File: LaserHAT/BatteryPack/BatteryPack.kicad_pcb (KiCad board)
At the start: 2 copper layers, 100 x 100 mm, 144 parts, among them J1 TYPE-C-31-M-12, J3 B4B-PH-K-S(LF)(SN), J5 S5B-XH-A-1(LF)(SN), J6 S5B-XH-A-1(LF)(SN), J7 XT60PW-M, J8 XT60PW-M, Q1 AO3401A, Q10 AO3400A, Q11 AO3400A, Q12 AO3400A, Q13 AO3401A, Q14 AO3400A, Q15 AO3400A, Q16 AO3400A, Q17 AO3400A, Q18 AO3400A, Q6 AO3401A, Q7 AO3400A, Q8 AO3400A, Q9 AO3400A, SW1 CAX-MTS203M-YB-10.6JL, U1 LM393DR2G, U10 HY2213-BB3A, U11 HY2213-BB3A, U12 HY2213-BB3A, U13 HY2213-BB3A, U14 LM393DR2G, U15 LM393DR2G, U16 CJ431, U2 LM393DR2G, U3 CJ431, U4 CH224A, U5 CN3704, U6 HY2213-BB3A, U7 HY2213-BB3A, U8 HY2213-BB3A, U9 HY2213-BB3A

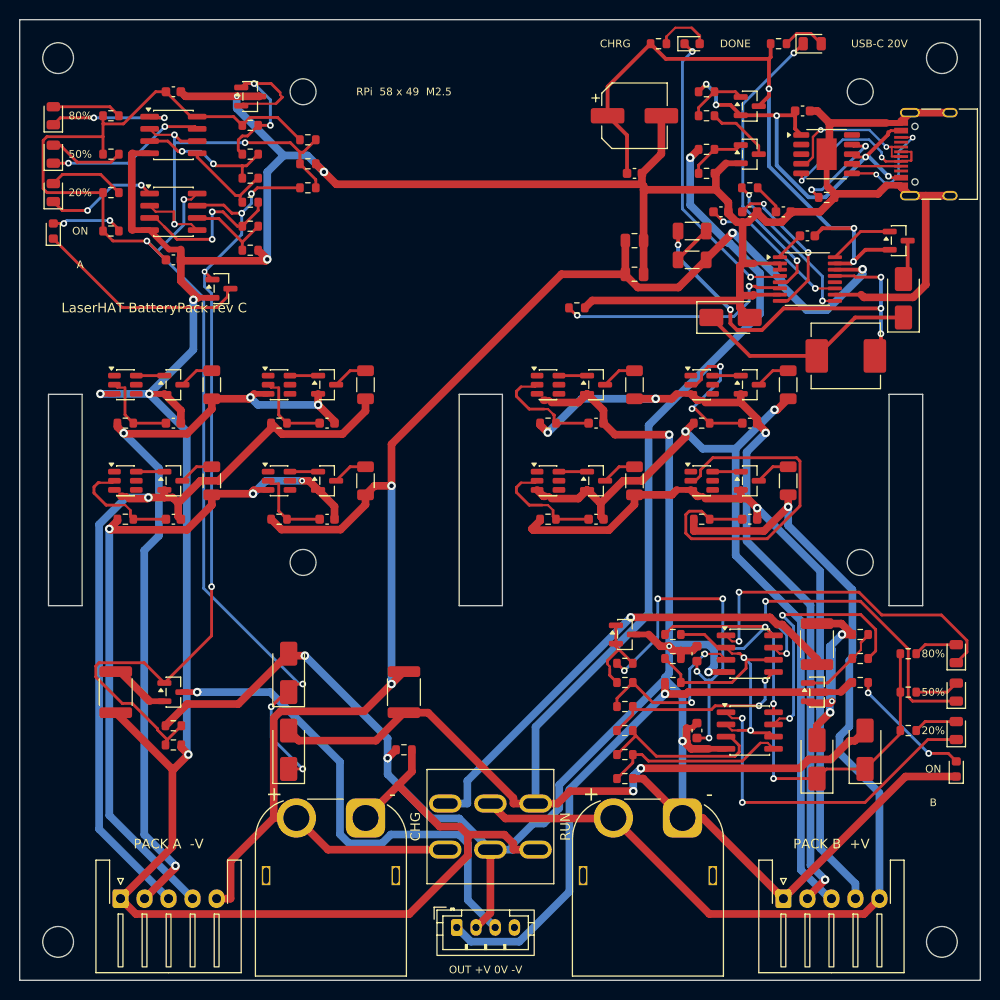
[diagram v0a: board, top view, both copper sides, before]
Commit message: BatteryPack: Pi rests along the front edge (H5-H8 at y 47.5 / 96.5) so the HAT's SW corner is over J3
The e-stim module's battery connector is at the HAT's south-west corner, so the Pi now sits over
y 44-100: toggle (13.5, 61.5, lever along y), J3 (13, 83.5) and chain A in the strip left of the
Pi; J5 left of standoff H7, J7 / J8 / J6 between H7 and H8 (44.5 / 61.5 / 69.5); gauge B LEDs on
the right edge at y 30-42 above the Pi; pack A's right balancer column one row up, clear of H5;
PACK A / B labels on the back silk under the sockets.  Re-routed (Freerouting, 0 unconnected,
stubs trimmed).  DRC 0/0/0, path / sync 0, fab outputs regenerated (136 placements, 44 BOM lines).

Co-Authored-By: Claude Fable 5.1 <noreply@anthropic.com>
Claude-Session: https://claude.ai/code/session_018vgLizGzYPynnY93ajvoVA
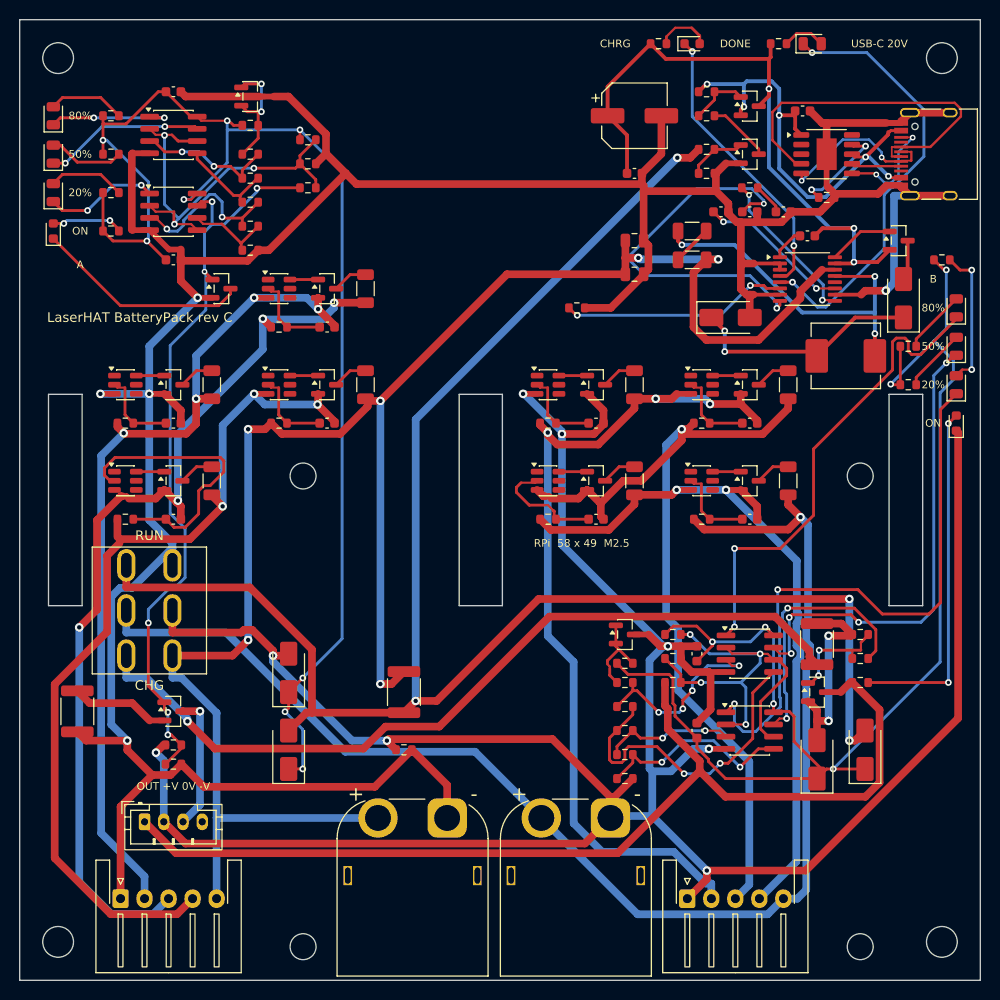
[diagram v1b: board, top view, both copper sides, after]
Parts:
- moved R55 49.1 mm to (96.0, 25.0)
- moved SW1 42.0 mm to (13.5, 61.5), turned to 90 degrees
- moved H5 40.0 mm to (29.5, 47.5)
- moved H6 40.0 mm to (87.5, 47.5)
- moved H7 40.0 mm to (29.5, 96.5)
- moved H8 40.0 mm to (87.5, 96.5)
- moved D11 36.0 mm to (97.5, 42.0)
- moved D12 36.0 mm to (97.5, 38.0)
- moved D13 36.0 mm to (97.5, 34.0)
- moved D14 36.0 mm to (97.5, 30.0)
- moved J3 34.3 mm to (13.0, 83.5)
- moved R56 32.0 mm to (92.5, 38.0)
- moved R57 32.0 mm to (92.5, 34.0)
- moved C13 10.0 mm to (32.0, 32.0)
- moved C15 10.0 mm to (32.0, 42.0)
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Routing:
- net 0V: track 211.1 -> 290.5 mm, vias 6 -> 8
- net +OUT: track 60.4 -> 108.6 mm, vias 1 -> 0
- net +GB: track 93.9 -> 140.4 mm, vias 8 -> 6
- net GND: track 401.4 -> 358.7 mm, vias 7 -> 5
- net /-V: track 51.4 -> 15.6 mm
- net +BATB: track 105.1 -> 140.7 mm
- net +RUN: track 50.5 -> 85.5 mm
- net +CHGB: track 151.2 -> 182.1 mm, vias 3 -> 4
- net Net-(U13-VDD): track 39.4 -> 8.68 mm
- net +BAT: track 168.8 -> 195.8 mm, vias 4 -> 6
- net Net-(D12-K): track 35.7 -> 62.7 mm
- net Net-(D11-A): track 13.2 -> 36.5 mm
- net Net-(U5-COM1): track 16.3 -> 39.3 mm
- net Net-(U4-DP): track 15.8 -> 38.5 mm, vias 2 -> 0
- net /C3: track 74.0 -> 94.8 mm
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
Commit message: BatteryPack: Pi turned 90 degrees along the left edge from the top-left corner
H5-H8 at (3.5 / 52.5, 81.5 / 23.5): the Pi lies over x 0-56, y 0-85 with its header on the
left edge, USB / Ethernet end over the top edge and SD card toward the front; the HAT then
covers x -1..56, y 20-85 and its south-west corner (e-stim module battery connector) is at
(56, 85), the module reaching x 65.  J3 (70, 63) and the toggle (74, 52) sit beside it in the
right column, both gauges' LED columns are on the right edge (B y 30-42, A y 64-76), the four
pack sockets in the front strip; under the Pi only the gauges' comparators (B's moved top
centre), the balancers (B's below A's) and the -V chain (above J7).  place.py has PI_ROT /
pi_xy() so the HAT outline (User.Comments) and Pi outline (User.Drawings) rotate with the
holes; title silk on the back.  Re-routed: Freerouting + maze router for four leftovers, GND
link at U5 pin 10 and three via nudges by hand.  DRC 0/0/0, path / sync 0, fab outputs
regenerated (136 placements, 44 BOM lines).

Co-Authored-By: Claude Fable 5.1 <noreply@anthropic.com>
Claude-Session: https://claude.ai/code/session_018vgLizGzYPynnY93ajvoVA
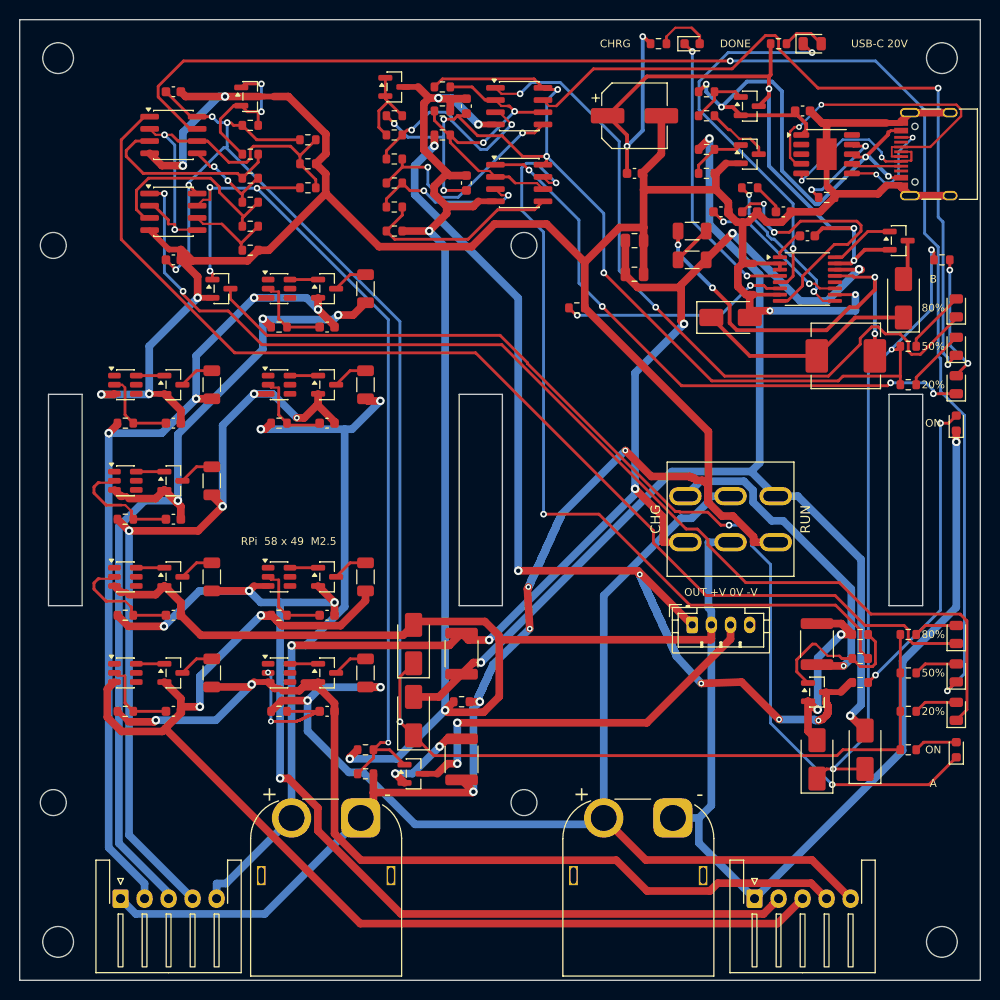
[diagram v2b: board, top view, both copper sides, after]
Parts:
- moved D1 108.4 mm to (97.5, 76.0)
- moved D2 108.4 mm to (97.5, 72.0)
- moved D3 108.4 mm to (97.5, 68.0)
- moved D4 108.4 mm to (97.5, 64.0)
- moved R12 99.0 mm to (92.5, 76.0)
- moved R13 99.0 mm to (92.5, 72.0)
- moved R14 99.0 mm to (92.5, 68.0)
- moved R15 99.0 mm to (92.5, 64.0)
- moved H6 87.4 mm to (3.50, 23.5)
- moved H8 81.0 mm to (52.5, 23.5)
- moved C20 61.8 mm to (46.5, 9.00)
- moved C21 61.8 mm to (46.5, 17.0)
- moved R45 61.8 mm to (39.0, 10.0)
- moved R46 61.8 mm to (39.0, 12.0)
- moved R47 61.8 mm to (39.0, 14.5)
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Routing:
- net Net-(D3-K): track 16.6 -> 153.8 mm
- net Net-(D2-K): track 11.9 -> 119.7 mm
- net Net-(D4-K): track 13.4 -> 120.0 mm, vias 2 -> 0
- net /D1_K: track 22.4 -> 109.0 mm, vias 0 -> 2
- net +CHGB: track 182.1 -> 117.8 mm, vias 4 -> 3
- net /CUT_OCB: track 27.0 -> 84.5 mm
- net +RUN: track 85.5 -> 34.4 mm
- net +G: track 139.7 -> 176.1 mm, vias 8 -> 5
- net GND: track 358.7 -> 394.1 mm, vias 5 -> 12
- net +GB: track 140.4 -> 172.7 mm, vias 6 -> 9
- net /B2: track 90.5 -> 121.4 mm, vias 1 -> 2
- net Net-(D13-K): track 49.6 -> 77.8 mm, vias 4 -> 2
- net /-V: track 15.6 -> 41.8 mm, vias 1 -> 2
- net Net-(D14-K): track 50.4 -> 75.2 mm
- net /B3: track 76.6 -> 100.6 mm
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
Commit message: BatteryPack: Pi turned so its USB-C / HDMI face is flush with the left edge, J3 in the top-left corner under the module's battery pads
The e-stim module hangs 9 mm past the HAT's south edge with its electrode header pointing south, and its battery pads
sit at its SW corner; that face is also the Pi's power / HDMI face.  The Pi now lies along the left edge over x 0-56,
y 15-100 (PI_ROT 270: H5-H8 at (3.5/52.5, 18.5/76.5), SD end up, USB / Ethernet over the front edge), so the
module overhangs the top-left corner (x -9..24, y 16-43) and the stimulation wires and Pi cables all leave over the
left edge instead of crossing the board.  J3 pin 1 at (4, 4), pins down to y 10, right below the module's battery
pads (x -3..3, y 16-23); H1 moved to (12, 4) for it; U15 / C21 to y 27, clear of H5.  The HAT's thumbwheel pokes
past the top edge at x 6.5-19, y 9-15, so the J3 cable stays west of it.  Re-routed (Freerouting, 0 unconnected),
DRC 0 / 0 / 0, path and sync 0, fab outputs and renders regenerated.

Co-Authored-By: Claude Fable 5.1 <noreply@anthropic.com>
Claude-Session: https://claude.ai/code/session_018vgLizGzYPynnY93ajvoVA
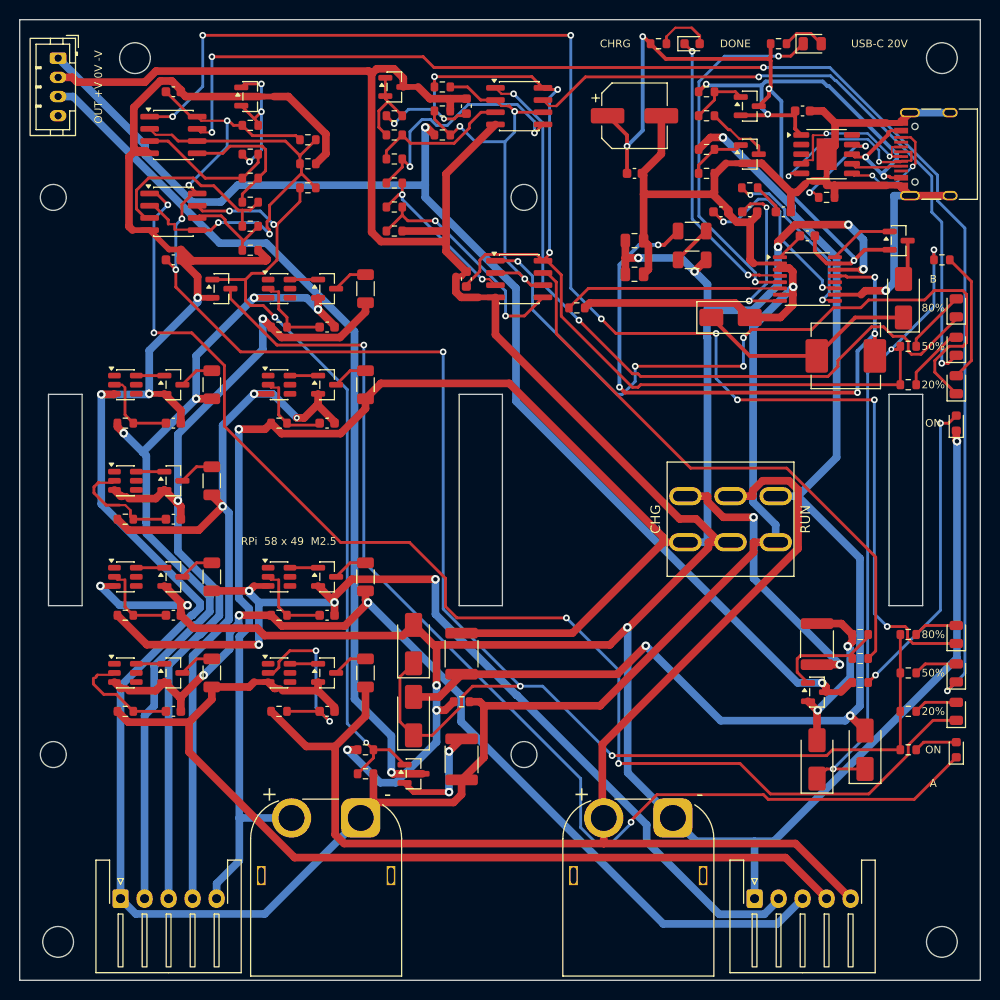
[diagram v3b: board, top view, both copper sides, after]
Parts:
- moved J3 88.5 mm to (4.00, 4.00), turned to -90 degrees
- moved H5 79.8 mm to (52.5, 18.5)
- moved H7 79.8 mm to (3.50, 18.5)
- moved H6 72.2 mm to (52.5, 76.5)
- moved H8 72.2 mm to (3.50, 76.5)
- moved C21 10.0 mm to (46.5, 27.0)
- moved U15 10.0 mm to (52.0, 27.0)
- moved H1 8.00 mm to (12.0, 4.00)
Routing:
- net /-V: track 41.8 -> 91.8 mm, vias 2 -> 1
- net 0V: track 291.5 -> 333.3 mm, vias 6 -> 7
- net Net-(D4-K): track 120.0 -> 148.6 mm, vias 0 -> 8
- net GND: track 394.1 -> 421.0 mm, vias 12 -> 5
- net +BAT: track 186.4 -> 211.6 mm, vias 8 -> 6
- net /CUT_OCB: track 84.5 -> 60.9 mm, vias 2 -> 0
- net /B2: track 121.4 -> 98.9 mm, vias 2 -> 3
- net /CSP: track 42.7 -> 64.6 mm, vias 4 -> 5
- net +OUT: track 106.2 -> 127.8 mm, vias 6 -> 2
- net Net-(U4-DP): track 34.5 -> 16.2 mm
- net Net-(D12-K): track 62.2 -> 77.7 mm
- net Net-(D2-K): track 119.7 -> 134.6 mm, vias 2 -> 4
- net +BATB: track 122.5 -> 135.0 mm, vias 2 -> 0
- net Net-(U5-COM1): track 28.4 -> 16.7 mm
- net /D1_K: track 109.0 -> 120.4 mm
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
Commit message: BatteryPack: toggle turned 90 degrees so its lever is parallel to the Pi (RUN up, CHARGE down)
SW1 at (74, 52) rot 90; re-routed (Freerouting + a hand-drawn front-layer link for U5 pad 10's GND, south of the
charger's pads to the GND trunk at x 75.5).  DRC 0 / 0 / 0, path and sync 0, fab outputs and renders regenerated.

Co-Authored-By: Claude Fable 5.1 <noreply@anthropic.com>
Claude-Session: https://claude.ai/code/session_018vgLizGzYPynnY93ajvoVA
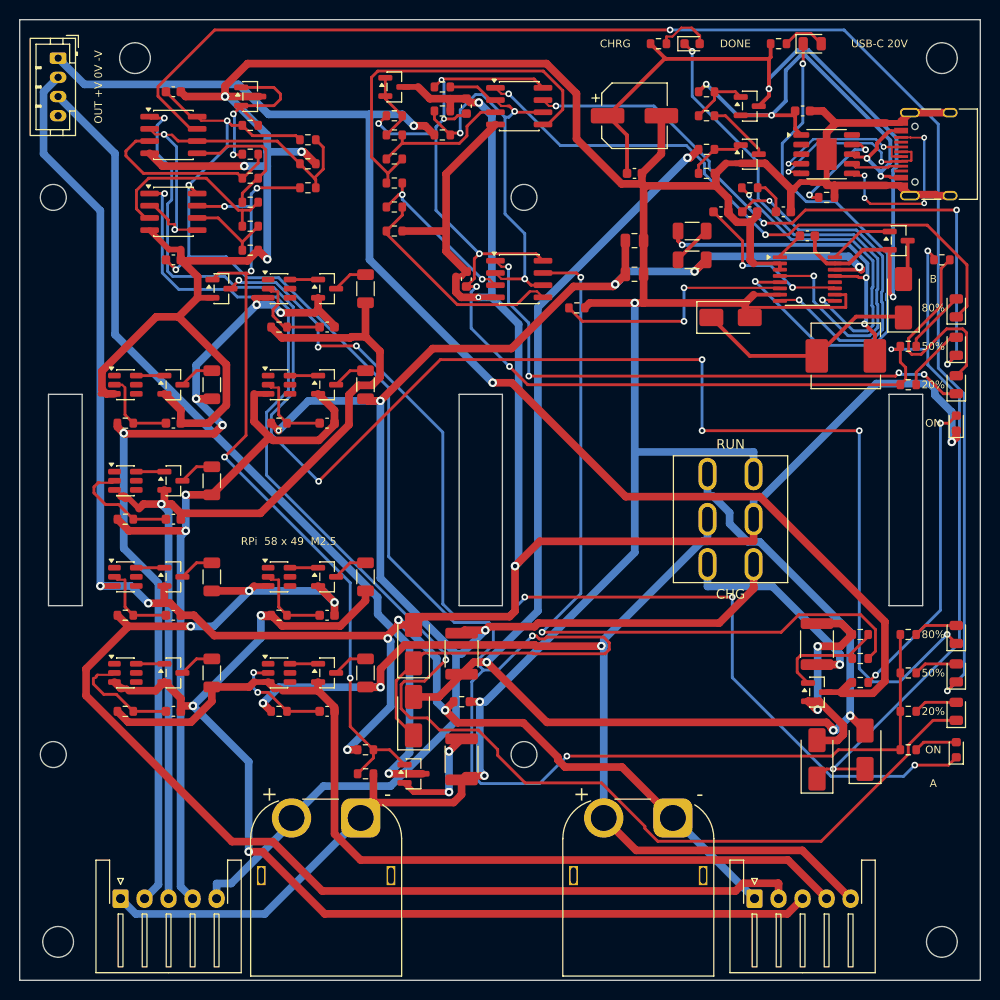
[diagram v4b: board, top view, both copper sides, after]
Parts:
- turned SW1 to 90 degrees
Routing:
- net +G: track 184.1 -> 215.3 mm, vias 7 -> 5
- net /CSP: track 64.6 -> 35.2 mm, vias 5 -> 3
- net +BATB: track 135.0 -> 107.0 mm, vias 0 -> 3
- net /CHRG: track 30.2 -> 56.3 mm
- net Net-(U5-COM1): track 16.7 -> 38.2 mm
- net +BAT: track 211.6 -> 190.3 mm
- net /CUT_OCB: track 60.9 -> 82.2 mm, vias 0 -> 2
- net /B1: track 105.5 -> 126.4 mm, vias 4 -> 3
- net +CHGB: track 128.5 -> 147.9 mm, vias 3 -> 4
- net /DONE: track 38.3 -> 57.0 mm
- net Net-(D12-K): track 77.7 -> 59.4 mm
- net /B2: track 98.9 -> 116.4 mm
- net VCHG: track 72.3 -> 86.9 mm, vias 4 -> 2
- net /TH50B: track 25.8 -> 39.6 mm, vias 2 -> 0
- net +OUT: track 127.8 -> 141.4 mm
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
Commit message: BatteryPack: gauge A's LEDs on the top edge beside its comparators, ICs turned by an orientation pass; re-routed
Gauge A's four LED nets ran ~150 mm each from its comparators (top left) to the right edge: D1-D4 now on the top edge at
x 20-32 with R12-R15 in a column at x 35, labels under them.  An orientation pass (ROT in place.py) tries every IC /
transistor at 0/90/180/270 and keeps the rotation with the shortest ratsnest that overlaps no courtyard (17 parts, ~1 mm
each).  Track 4486 -> 3812 mm, 1253 -> 1121 segments, 143 -> 137 vias.  Freerouting + a hand-drawn link for U5 pad 10's
GND (east, down the back layer, across to the GND trunk at x 76.4).  DRC 0 / 0 / 0, path and sync 0, fab outputs and
renders regenerated.

Co-Authored-By: Claude Fable 5.1 <noreply@anthropic.com>
Claude-Session: https://claude.ai/code/session_018vgLizGzYPynnY93ajvoVA
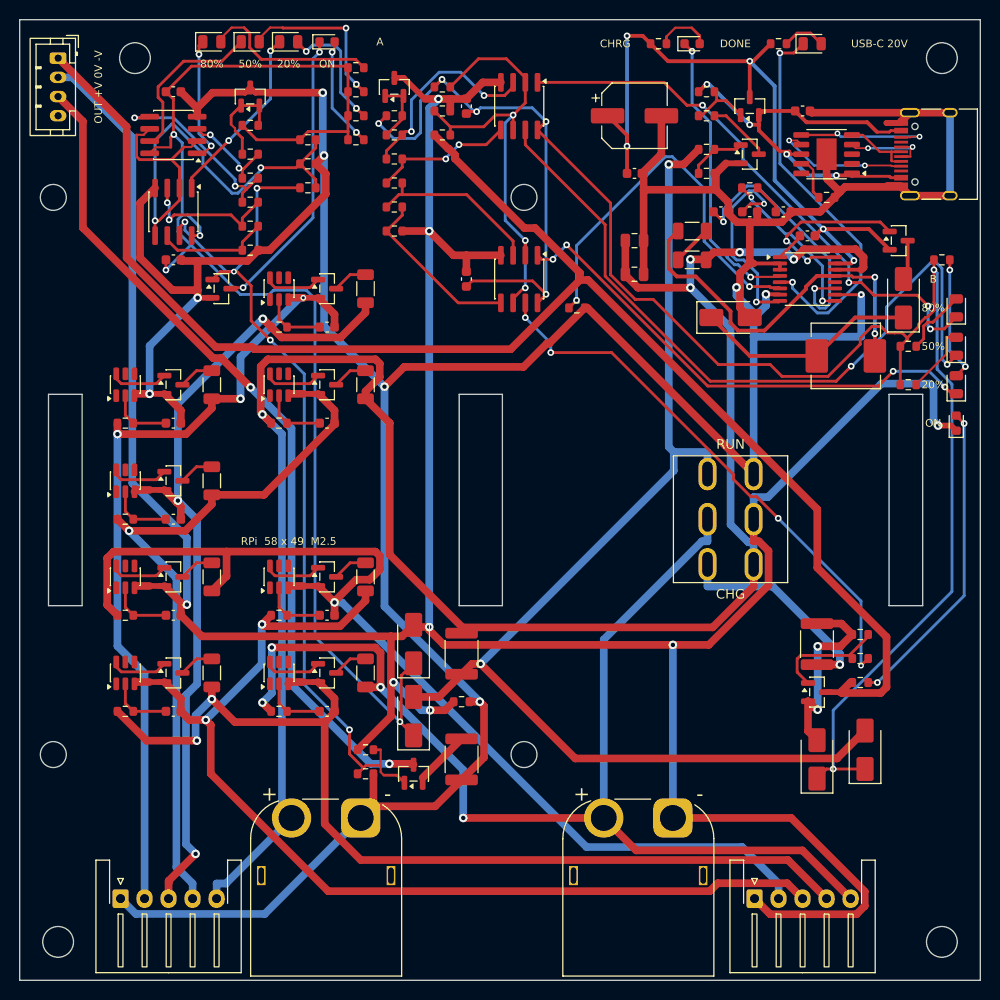
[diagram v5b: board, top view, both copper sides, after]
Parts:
- moved D4 99.1 mm to (20.0, 2.30), turned to 0 degrees
- moved D1 98.6 mm to (32.0, 2.30), turned to 0 degrees
- moved D3 98.6 mm to (24.0, 2.30), turned to 0 degrees
- moved D2 98.4 mm to (28.0, 2.30), turned to 0 degrees
- moved R12 85.7 mm to (35.0, 12.5)
- moved R13 84.6 mm to (35.0, 10.0)
- moved R14 83.5 mm to (35.0, 7.50)
- moved R15 82.4 mm to (35.0, 5.00)
- turned Q11 to 90 degrees
- turned Q13 to 90 degrees
- turned U1 to 180 degrees
- turned U10 to 90 degrees
- turned U11 to 90 degrees
- turned U12 to 90 degrees
- turned U13 to 90 degrees
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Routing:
- net Net-(D4-K): track 161.2 -> 13.3 mm, vias 6 -> 2
- net Net-(D3-K): track 156.4 -> 17.3 mm, vias 2 -> 0
- net Net-(D2-K): track 147.8 -> 19.0 mm
- net /D1_K: track 116.8 -> 30.3 mm, vias 6 -> 2
- net +G: track 215.3 -> 141.7 mm, vias 5 -> 4
- net /CHRG: track 56.3 -> 30.5 mm
- net /CUT_OCB: track 82.2 -> 57.3 mm, vias 2 -> 4
- net /TH50B: track 39.6 -> 14.8 mm, vias 0 -> 2
- net +CHGB: track 147.9 -> 123.8 mm, vias 4 -> 2
- net +OUT: track 141.4 -> 164.2 mm, vias 2 -> 0
- net +BAT: track 190.3 -> 211.3 mm, vias 6 -> 5
- net Net-(U5-COM1): track 38.2 -> 21.3 mm
- net /DONE: track 57.0 -> 41.5 mm
- net Net-(U5-COM2): track 31.9 -> 16.9 mm
- net Net-(U5-TEMP): track 26.1 -> 40.7 mm
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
